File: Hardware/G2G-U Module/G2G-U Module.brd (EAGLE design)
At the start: 100 x 80 mm, 4 parts, among them J1 GROVE-4P-2.0-SMD-FEMALE-REINF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

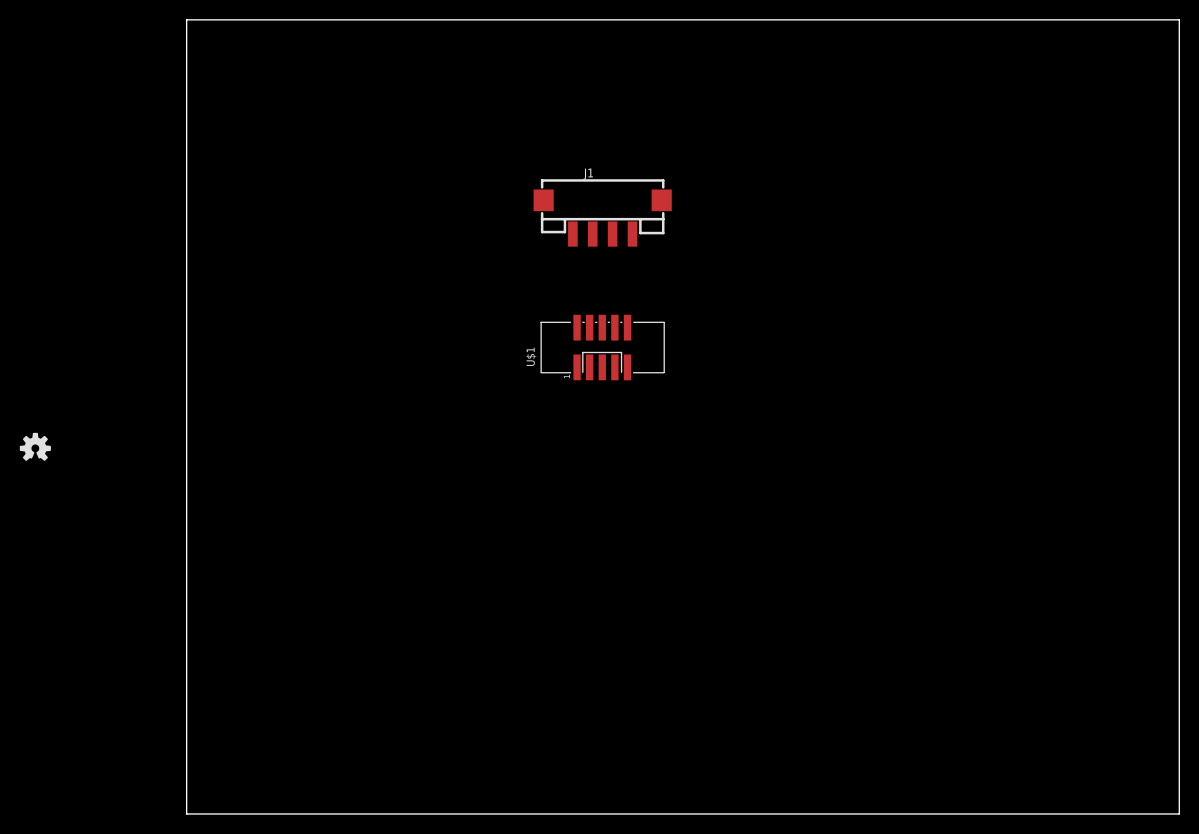
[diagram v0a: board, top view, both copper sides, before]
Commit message: First draft of G2G-U before ground plane.
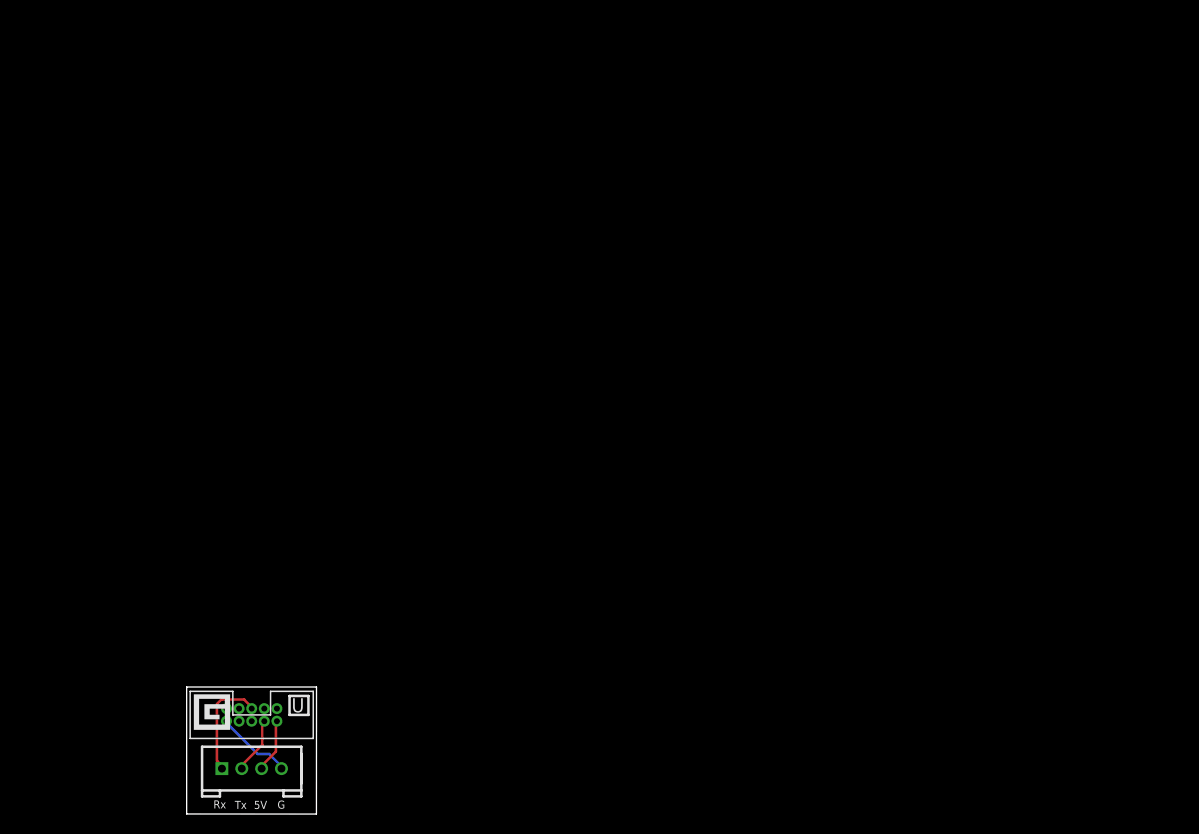
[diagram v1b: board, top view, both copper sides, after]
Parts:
- removed FRAME1: FRAME-LETTER, SparkFun-Aesthetics:CREATIVE_COMMONS
- J1: value GROVE-4P-2.0-SMD-FEMALE-REINFORCE-3470090P1 -> GROVE-4P-2.0-3470130P1; device Connector:4P-SMD-2.0 -> SoftDust:4P-2.0
- U$1: value GADGETEER-SOCKET -> 2X5_1.27MM_FEMALE_PLUG; device SoftDust:2X5_1.27MM -> SoftDust:2X5_1.27MM_FEMALE_PLUG
- moved J1 64.4 mm to (6.55, 4.57)
- moved U$1 51.2 mm to (6.55, 9.98), flipped to the bottom, turned to 0 degrees
- moved LOGO1 39.0 mm to (1.88, 1.78), flipped to the bottom
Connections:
- net N$1 renamed RX
- net N$2 renamed TX
- net N$3 renamed +5V
- net N$4 renamed GND
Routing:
- net RX: track 0.00 -> 10.9 mm
- net GND: track 0.00 -> 7.74 mm
- net TX: track 0.00 -> 5.75 mm
- net +5V: track 0.00 -> 5.39 mm
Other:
- board size 100 x 80 mm -> 13.1 x 12.8 mm
- board text added: "5V"
- board text added: "G"
- board text added: "G2G-U"
- board text added: "Rx"
- board text added: "Tx"
- board text added: "U"
- board text added: "http://gadgeteer.in"
- board text added: "v1.0"
